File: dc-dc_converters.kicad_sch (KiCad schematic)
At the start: 61 parts, among them J3 JST_SH_1x4_SM04B-SRSS-TB-LF-SN, J4 Molex_Nano-Fit_1x2_105313-220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, U2 SIC477ED-T1-GE3, U3 AP62301WU-7, U4 AP62301WU-7

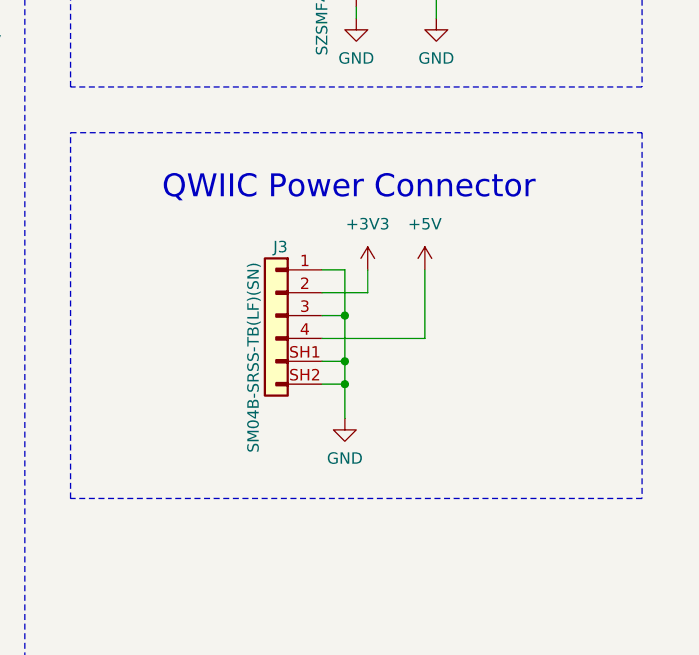
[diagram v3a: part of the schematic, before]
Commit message: [#57006] Remove buses to improve readability
Change output power block's name
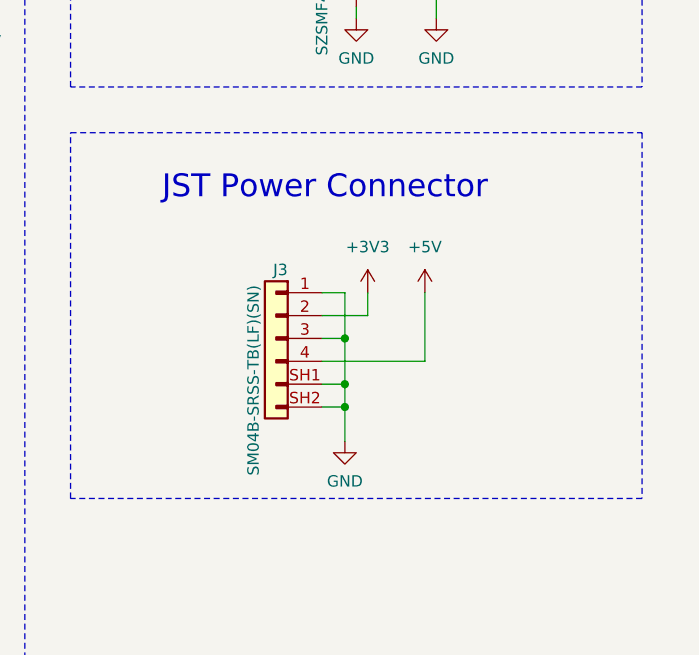
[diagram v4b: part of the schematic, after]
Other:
- note added: "JST Power Connector"
- note removed: "QWIIC Power Connector"
- moved on the sheet: J3
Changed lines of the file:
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@@
   (junction (at 193.04 73.66) (diameter 0) (color 0 0 0 0)
   )
-  (junction (at 304.8 101.6) (diameter 0) (color 0 0 0 0)
+  (junction (at 304.8 104.14) (diameter 0) (color 0 0 0 0)
   )
   (junction (at 189.23 92.71) (diameter 0) (color 0 0 0 0)
@@
   (junction (at 167.64 81.28) (diameter 0) (color 0 0 0 0)
   )
-  (junction (at 304.8 96.52) (diameter 0) (color 0 0 0 0)
+  (junction (at 304.8 99.06) (diameter 0) (color 0 0 0 0)
   )
   (junction (at 144.78 90.17) (diameter 0) (color 0 0 0 0)
   )
-  (junction (at 304.8 104.14) (diameter 0) (color 0 0 0 0)
+  (junction (at 304.8 106.68) (diameter 0) (color 0 0 0 0)
   )
   (junction (at 71.12 175.26) (diameter 0) (color 0 0 0 0)
@@
     (stroke (width 0) (type default))
   )
-  (wire (pts (xy 304.8 101.6) (xy 302.26 101.6))
+  (wire (pts (xy 304.8 104.14) (xy 302.26 104.14))
     (stroke (width 0) (type default))
   )
@@
     (stroke (width 0) (type default))
   )
-  (wire (pts (xy 304.8 104.14) (xy 304.8 101.6))
+  (wire (pts (xy 304.8 106.68) (xy 304.8 104.14))
     (stroke (width 0) (type default))
   )
@@
     (stroke (width 0) (type default))
   )
-  (wire (pts (xy 302.26 91.44) (xy 304.8 91.44))
+  (wire (pts (xy 302.26 93.98) (xy 304.8 93.98))
     (stroke (width 0) (type default))
   )
@@
     (stroke (width 0) (type default))
   )
-  (wire (pts (xy 304.8 91.44) (xy 304.8 96.52))
+  (wire (pts (xy 304.8 93.98) (xy 304.8 99.06))
     (stroke (width 0) (type default))
   )
@@
     (stroke (width 0) (type default))
   )
-  (wire (pts (xy 304.8 104.14) (xy 304.8 107.95))
+  (wire (pts (xy 304.8 106.68) (xy 304.8 110.49))
     (stroke (width 0) (type default))
   )
@@
     (stroke (width 0) (type default))
   )
-  (wire (pts (xy 313.69 99.06) (xy 313.69 91.44))
+  (wire (pts (xy 313.69 101.6) (xy 313.69 93.98))
     (stroke (width 0) (type default))
   )
@@
     (stroke (width 0) (type default))
   )
-  (wire (pts (xy 302.26 99.06) (xy 313.69 99.06))
+  (wire (pts (xy 302.26 101.6) (xy 313.69 101.6))
     (stroke (width 0) (type default))
   )
@@
     (stroke (width 0) (type default))
   )
-  (wire (pts (xy 302.26 93.98) (xy 307.34 93.98))
+  (wire (pts (xy 302.26 96.52) (xy 307.34 96.52))
     (stroke (width 0) (type default))
   )
@@
     (stroke (width 0) (type default))
   )
-  (wire (pts (xy 304.8 96.52) (xy 304.8 101.6))
+  (wire (pts (xy 304.8 99.06) (xy 304.8 104.14))
     (stroke (width 0) (type default))
   )
@@
     (stroke (width 0) (type default))
   )
-  (wire (pts (xy 307.34 91.44) (xy 307.34 93.98))
+  (wire (pts (xy 307.34 93.98) (xy 307.34 96.52))
     (stroke (width 0) (type default))
   )
@@
     (stroke (width 0) (type default))
   )
-  (wire (pts (xy 302.26 96.52) (xy 304.8 96.52))
+  (wire (pts (xy 302.26 99.06) (xy 304.8 99.06))
     (stroke (width 0) (type default))
   )
@@
     (stroke (width 0) (type default))
   )
-  (wire (pts (xy 302.26 104.14) (xy 304.8 104.14))
+  (wire (pts (xy 302.26 106.68) (xy 304.8 106.68))
     (stroke (width 0) (type default))
   )
@@
     (effects (font (size 1.27 1.27)) (justify left bottom))
   )
-  (text "QWIIC Power Connector" (at 284.48 83.82 0)
+  (text "JST Power Connector" (at 284.48 83.82 0)
     (effects (font (size 2.54 2.54)) (justify left bottom))
   )
@@
     )
   )
-  (symbol (lib_id "antmicropower:+3V3") (at 307.34 91.44 0) (unit 1)
+  (symbol (lib_id "antmicropower:+3V3") (at 307.34 93.98 0) (unit 1)
     (in_bom yes) (on_board yes) (dnp no) (fields_autoplaced)
-    (property "Reference" "#PWR071" (at 322.58 91.44 0)
+    (property "Reference" "#PWR071" (at 322.58 93.98 0)
       (effects (font (size 1.27 1.27) (thickness 0.15)) (justify left bottom) hide)
     )
-    (property "Value" "+3V3" (at 307.34 86.36 0)
+    (property "Value" "+3V3" (at 307.34 88.9 0)
       (effects (font (size 1.27 1.27) (thickness 0.15)))
     )
-    (property "Footprint" "" (at 322.58 99.06 0)
+    (property "Footprint" "" (at 322.58 101.6 0)
       (effects (font (size 1.27 1.27) (thickness 0.15)) (justify left bottom) hide)
     )
-    (property "Datasheet" "" (at 322.58 101.6 0)
+    (property "Datasheet" "" (at 322.58 104.14 0)
       (effects (font (size 1.27 1.27) (thickness 0.15)) (justify left bottom) hide)
     )
-    (property "Author" "Antmicro" (at 322.58 93.98 0)
+    (property "Author" "Antmicro" (at 322.58 96.52 0)
       (effects (font (size 1.27 1.27) (thickness 0.15)) (justify left bottom) hide)
     )
-    (property "License" "Apache-2.0" (at 322.58 96.52 0)
+    (property "License" "Apache-2.0" (at 322.58 99.06 0)
       (effects (font (size 1.27 1.27) (thickness 0.15)) (justify left bottom) hide)
     )
@@
     )
   )
-  (symbol (lib_id "antmicropower:+5V") (at 313.69 91.44 0) (unit 1)
+  (symbol (lib_id "antmicropower:+5V") (at 313.69 93.98 0) (unit 1)
     (in_bom yes) (on_board yes) (dnp no) (fields_autoplaced)
-    (property "Reference" "#PWR072" (at 328.93 93.98 0)
+    (property "Reference" "#PWR072" (at 328.93 96.52 0)
       (effects (font (size 1.27 1.27) (thickness 0.15)) (justify left bottom) hide)
     )
-    (property "Value" "+5V" (at 313.69 86.36 0)
+    (property "Value" "+5V" (at 313.69 88.9 0)
       (effects (font (size 1.27 1.27) (thickness 0.15)))
     )
-    (property "Footprint" "" (at 328.93 99.06 0)
+    (property "Footprint" "" (at 328.93 101.6 0)
       (effects (font (size 1.27 1.27) (thickness 0.15)) (justify left bottom) hide)
     )
-    (property "Datasheet" "" (at 328.93 101.6 0)
+    (property "Datasheet" "" (at 328.93 104.14 0)
       (effects (font (size 1.27 1.27) (thickness 0.15)) (justify left bottom) hide)
     )
-    (property "Author" "Antmicro" (at 328.93 99.06 0)
+    (property "Author" "Antmicro" (at 328.93 101.6 0)
       (effects (font (size 1.27 1.27) (thickness 0.15)) (justify left bottom) hide)
     )
-    (property "License" "Apache-2.0" (at 328.93 101.6 0)
+    (property "License" "Apache-2.0" (at 328.93 104.14 0)
       (effects (font (size 1.27 1.27) (thickness 0.15)) (justify left bottom) hide)
     )
@@
     )
   )
-  (symbol (lib_id "antmicropower:GND") (at 304.8 107.95 0) (unit 1)
+  (symbol (lib_id "antmicropower:GND") (at 304.8 110.49 0) (unit 1)
     (in_bom yes) (on_board yes) (dnp no) (fields_autoplaced)
-    (property "Reference" "#PWR055" (at 304.8 107.95 0)
+    (property "Reference" "#PWR055" (at 304.8 110.49 0)
       (effects (font (size 1.27 1.27)) (justify left) hide)
     )
-    (property "Value" "GND" (at 304.8 112.395 0)
+    (property "Value" "GND" (at 304.8 114.935 0)
       (effects (font (size 1.27 1.27)))
     )
-    (property "Footprint" "" (at 304.8 107.95 0)
+    (property "Footprint" "" (at 304.8 110.49 0)
       (effects (font (size 1.27 1.27)) (justify left) hide)
     )
-    (property "Datasheet" "" (at 304.8 107.95 0)
+    (property "Datasheet" "" (at 304.8 110.49 0)
       (effects (font (size 1.27 1.27)) (justify left) hide)
     )
-    (property "Author" "Antmicro" (at 313.69 115.57 0)
+    (property "Author" "Antmicro" (at 313.69 118.11 0)
       (effects (font (size 1.27 1.27) (thickness 0.15)) (justify left bottom) hide)
     )
-    (property "License" "Apache-2.0" (at 313.69 118.11 0)
+    (property "License" "Apache-2.0" (at 313.69 120.65 0)
       (effects (font (size 1.27 1.27) (thickness 0.15)) (justify left bottom) hide)
     )
@@
     )
   )
-  (symbol (lib_id "antmicroWire2BoardConnectors:JST_SH_1x4_SM04B-SRSS-TB-LF-SN") (at 302.26 91.44 0) (mirror y) (unit 1)
+  (symbol (lib_id "antmicroWire2BoardConnectors:JST_SH_1x4_SM04B-SRSS-TB-LF-SN") (at 302.26 93.98 0) (mirror y) (unit 1)
     (in_bom yes) (on_board yes) (dnp no)
-    (property "Reference" "J3" (at 298.45 88.9 0)
+    (property "Reference" "J3" (at 298.45 91.44 0)
       (effects (font (size 1.27 1.27) (thickness 0.15)) (justify left))
     )
-    (property "Value" "JST_SH_1x4_SM04B-SRSS-TB-LF-SN" (at 275.59 99.06 0)
+    (property "Value" "JST_SH_1x4_SM04B-SRSS-TB-LF-SN" (at 275.59 101.6 0)
       (effects (font (size 1.27 1.27) (thickness 0.15)) (justify left bottom) hide)
     )
-    (property "Footprint" "antmicro-footprints:Conn_JST_SH_1x4_SM04B-SRSS-TB-LF-SN" (at 275.59 101.6 0)
+    (property "Footprint" "antmicro-footprints:Conn_JST_SH_1x4_SM04B-SRSS-TB-LF-SN" (at 275.59 104.14 0)
       (effects (font (size 1.27 1.27) (thickness 0.15)) (justify left bottom) hide)
     )
-    (property "Datasheet" "https://www.jst-mfg.com/product/pdf/eng/eSH.pdf" (at 275.59 104.14 0)
+    (property "Datasheet" "https://www.jst-mfg.com/product/pdf/eng/eSH.pdf" (at 275.59 106.68 0)
       (effects (font (size 1.27 1.27) (thickness 0.15)) (justify left bottom) hide)
     )
-    (property "MPN" "SM04B-SRSS-TB(LF)(SN)" (at 294.64 111.76 90)
+    (property "MPN" "SM04B-SRSS-TB(LF)(SN)" (at 294.64 114.3 90)
       (effects (font (size 1.27 1.27) (thickness 0.15)) (justify left))
     )
-    (property "Manufacturer" "JST Automotive Connectors" (at 275.59 106.68 0)
+    (property "Manufacturer" "JST Automotive Connectors" (at 275.59 109.22 0)
       (effects (font (size 1.27 1.27) (thickness 0.15)) (justify left bottom) hide)
     )
-    (property "Author" "Antmicro" (at 275.59 109.22 0)
+    (property "Author" "Antmicro" (at 275.59 111.76 0)
       (effects (font (size 1.27 1.27) (thickness 0.15)) (justify left bottom) hide)
     )
-    (property "License" "Apache-2.0" (at 275.59 111.76 0)
+    (property "License" "Apache-2.0" (at 275.59 114.3 0)
       (effects (font (size 1.27 1.27) (thickness 0.15)) (justify left bottom) hide)
     )

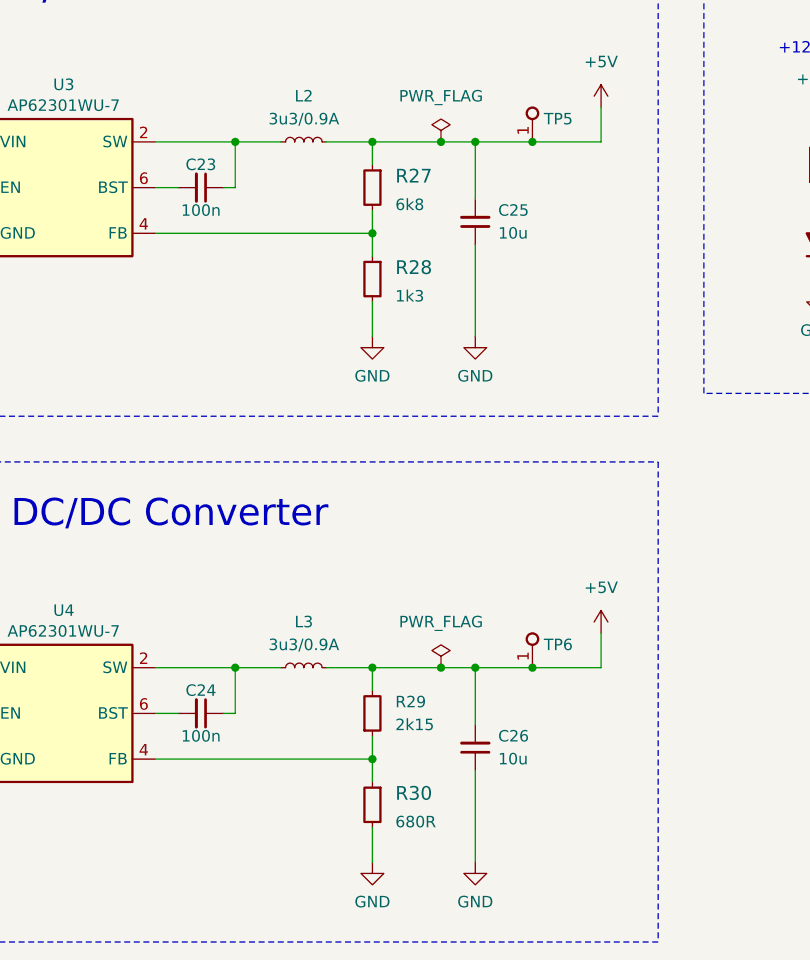
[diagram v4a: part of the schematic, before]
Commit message: [#57006] Change feedback resistors for U3, U4
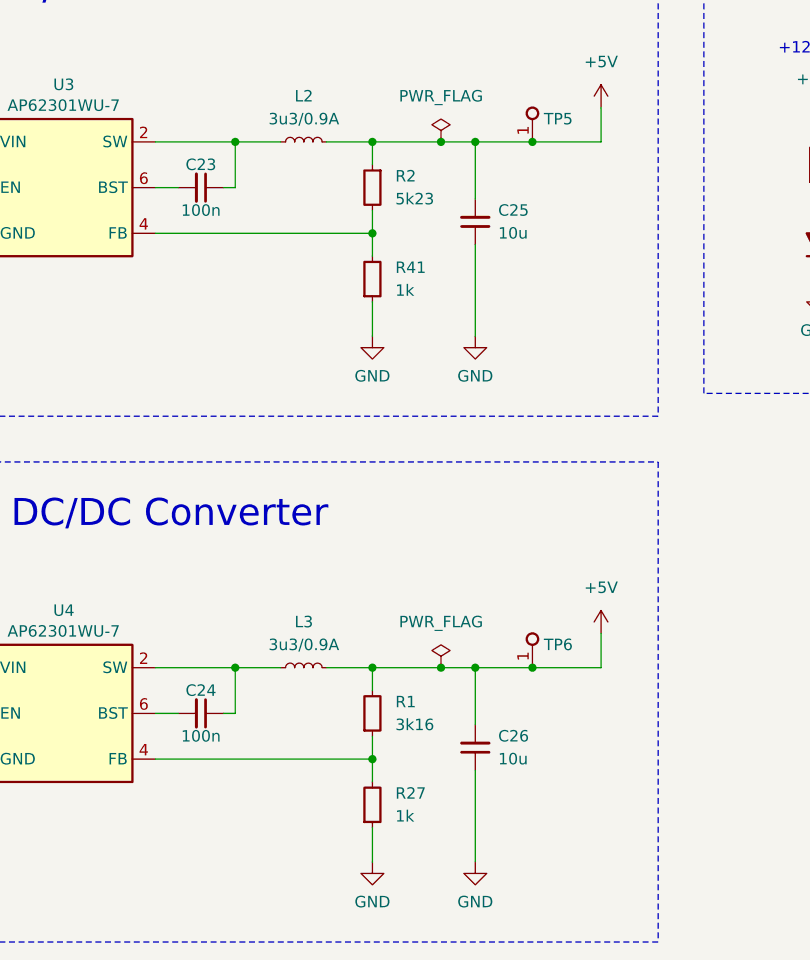
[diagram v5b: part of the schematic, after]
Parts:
- removed R27: R_6k8_0402, antmicro-footprints:R_0402_1005Metric, symbol antmicroResistors0402:R_6k8_0402
- removed R28: R_1k3_0402, antmicro-footprints:R_0402_1005Metric, symbol antmicroResistors0402:R_1k3_0402
- removed R29: R_template_name_0402, antmicro-footprints:R_0402_1005Metric, symbol antmicroResistors0402:R_2k15_0402
- removed R30: R_680R_0402, antmicro-footprints:R_0402_1005Metric, symbol antmicroResistors0402:R_680R_0402
- added R1: R_3k16_0402, antmicro-footprints:R_0402_1005Metric, symbol antmicroResistors0402:R_3k16_0402
- added R2: R_5k23_0402, antmicro-footprints:R_0402_1005Metric, symbol antmicroResistors0402:R_5k23_0402
- added R27, R41: R_1k_0402, antmicro-footprints:R_0402_1005Metric, symbol antmicroResistors0402:R_1k_0402
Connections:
- net +5V: now also R1.2, R2.1
- net GND: now also R27.1, R41.1
- net at U3.4 (FB): now also R2.2, R41.2
- net at U4.4 (FB): now also R1.1, R27.2
